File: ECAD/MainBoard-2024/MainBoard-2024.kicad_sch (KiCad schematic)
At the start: 60 parts, among them J1 XT60, J11 Conn_01x03, J12 Conn_01x04, J13 Conn_01x03, J14 Conn_01x03, J16 XT30, J17 XT30, J2 Conn_01x04, J20 BAU, J21 BAU, J22 Conn_01x04, J23 Conn_01x02, J26 BAU, J27 BAU, J28 Conn_01x02, J29 Conn_01x02, J3 ConStep1, J30 Conn_01x03, J5 ConStep1, J6 ConStep1, J7 XT30, J8 Conn_01x02, K2 FINDER-36.11, U1 Teensy3.5_All_Pins, U2 R-78B3.3-2.0, U3 R-78B12-2.0, U4 R-78B5.0-2.0

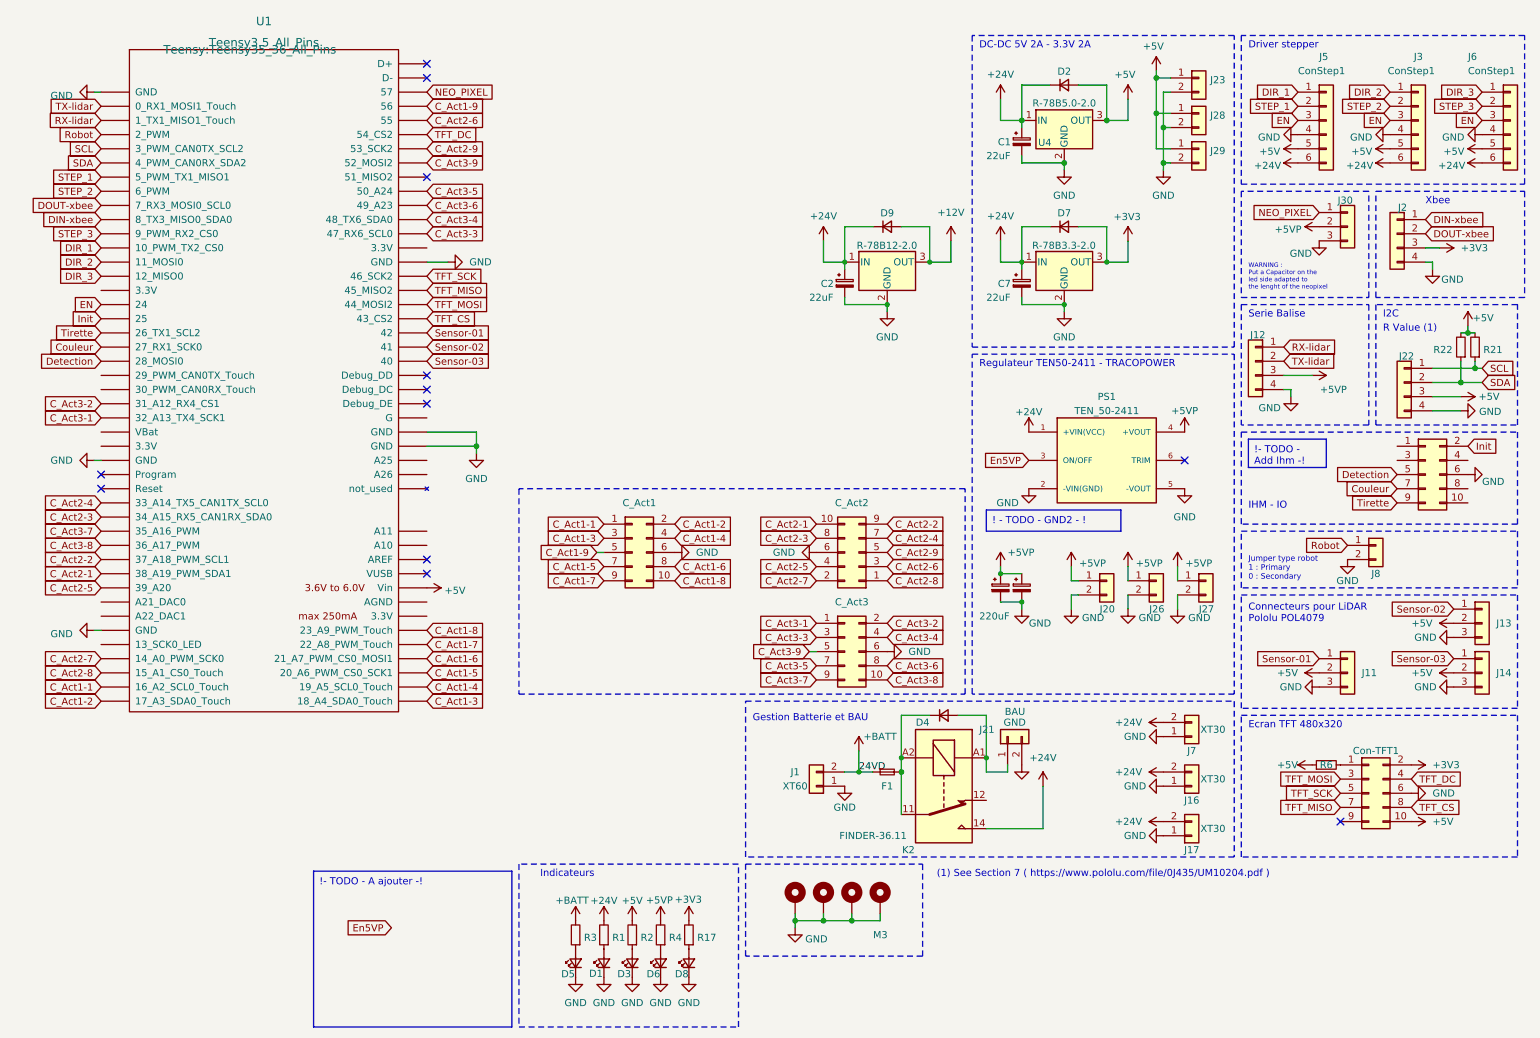
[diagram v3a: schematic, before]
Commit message: add ihm features and 12V connectores
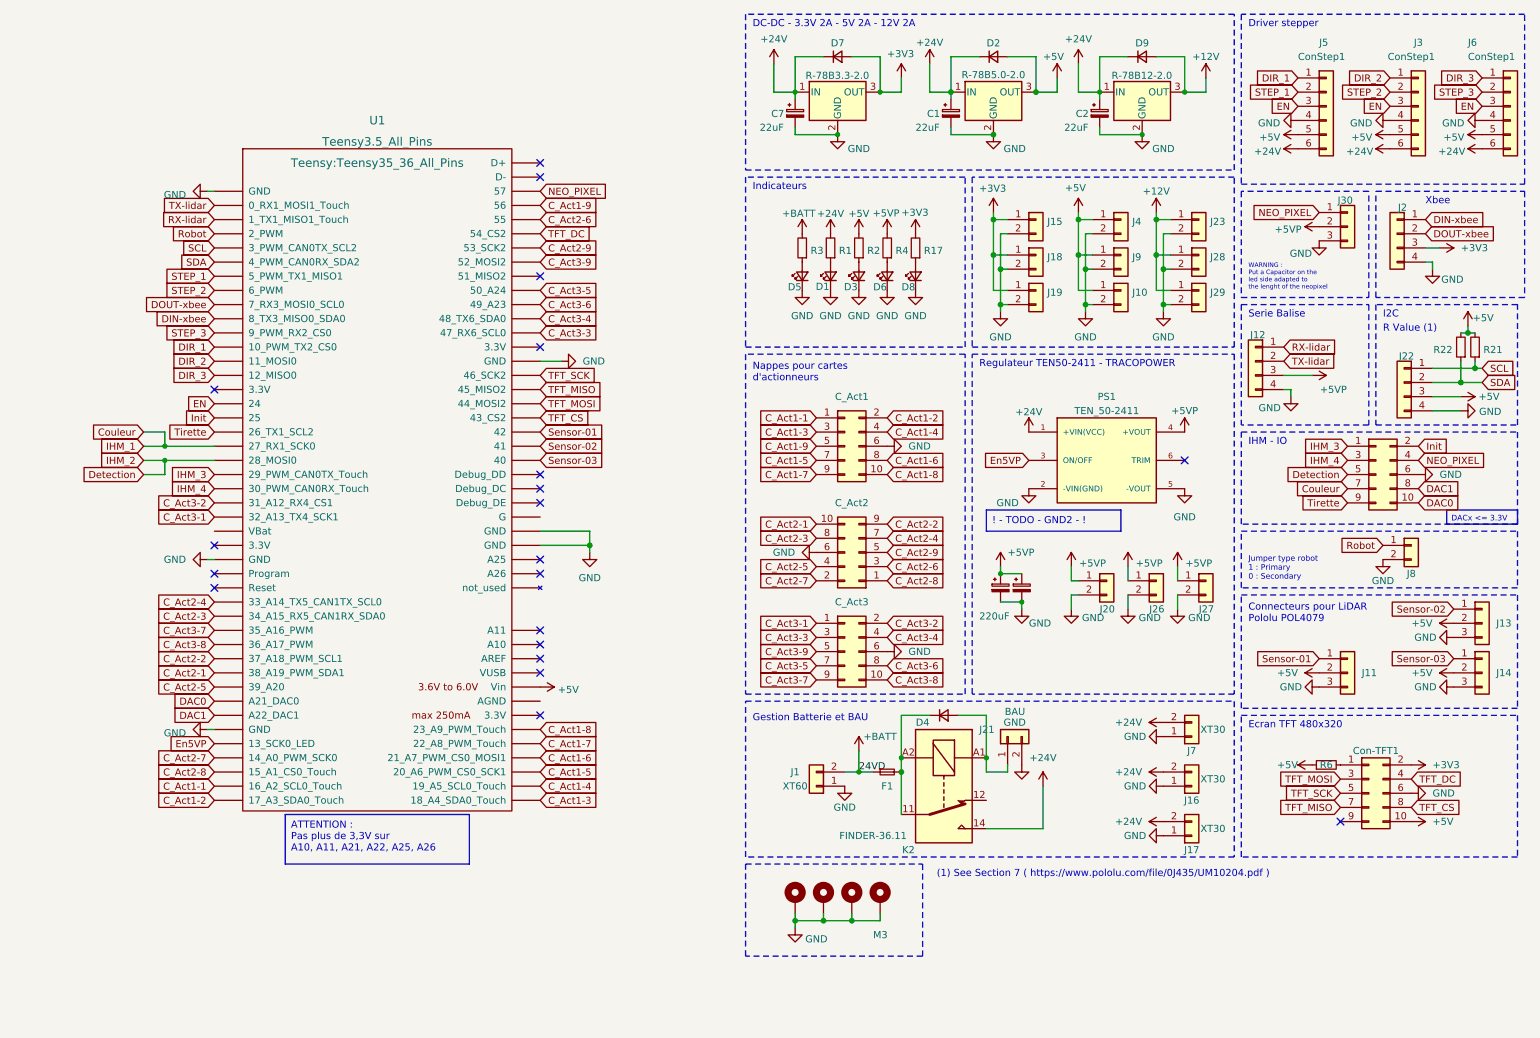
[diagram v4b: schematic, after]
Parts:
- added J10, J15, J18, J19, J4, J9: Conn_01x02, Connector_Molex:Molex_KK-254_AE-6410-02A_1x02_P2.54mm_Vertical, symbol Connector_Generic:Conn_01x02
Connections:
- net +12V: now also J23.1 (Pin_1), J28.1 (Pin_1), J29.1 (Pin_1)
- net +3V3: now also J15.1 (Pin_1), J18.1 (Pin_1), J19.1 (Pin_1)
- net +5V: now also J10.1 (Pin_1), J4.1 (Pin_1), J9.1 (Pin_1); no longer J23.1 (Pin_1), J28.1 (Pin_1), J29.1 (Pin_1)
- net En5VP: now also U1.40 (13_SCK0_LED)
- net GND: now also J10.2 (Pin_2), J15.2 (Pin_2), J18.2 (Pin_2), J19.2 (Pin_2), J4.2 (Pin_2), J9.2 (Pin_2)
- net NEO_PIXEL: now also IHM-IO1.4 (Pin_4)
- net IHM_3: now reaches IHM-IO1.1 (Pin_1)
- net IHM_3: now also U1.21 (29_PWM_CAN0TX_Touch)
- net DAC0: now reaches IHM-IO1.10 (Pin_10)
- net DAC0: now also U1.37 (A21_DAC0)
- net IHM_4: now reaches IHM-IO1.3 (Pin_3)
- net IHM_4: now also U1.22 (30_PWM_CAN0RX_Touch)
- net DAC1: now reaches IHM-IO1.8 (Pin_8)
- net DAC1: now also U1.38 (A22_DAC1)
- no-connect marks 12 -> 20
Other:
- note added: "DC-DC - 3.3V 2A - 5V 2A - 12V 2A"
- note added: "Nappes pour cartes d'actionneurs"
- note removed: "DC-DC 5V 2A - 3.3V 2A"
- moved on the sheet: C1, C2, C7, C_Act1, D1, D2, D3, D5, D6, D7, D8, D9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

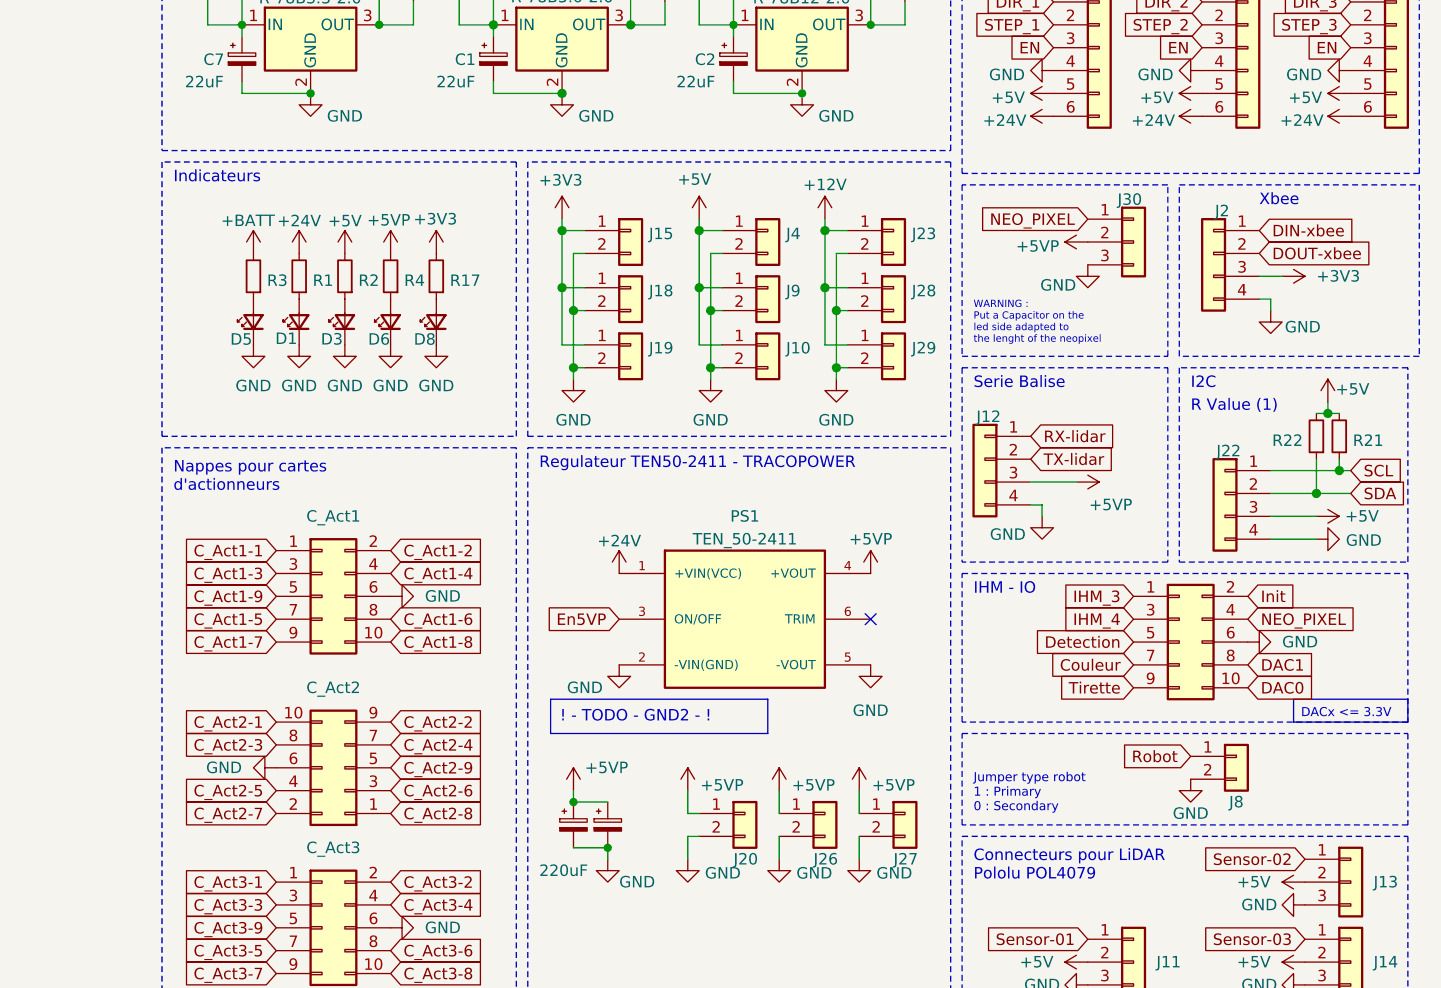
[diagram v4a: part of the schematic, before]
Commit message: Update 3.3V connectors and placements
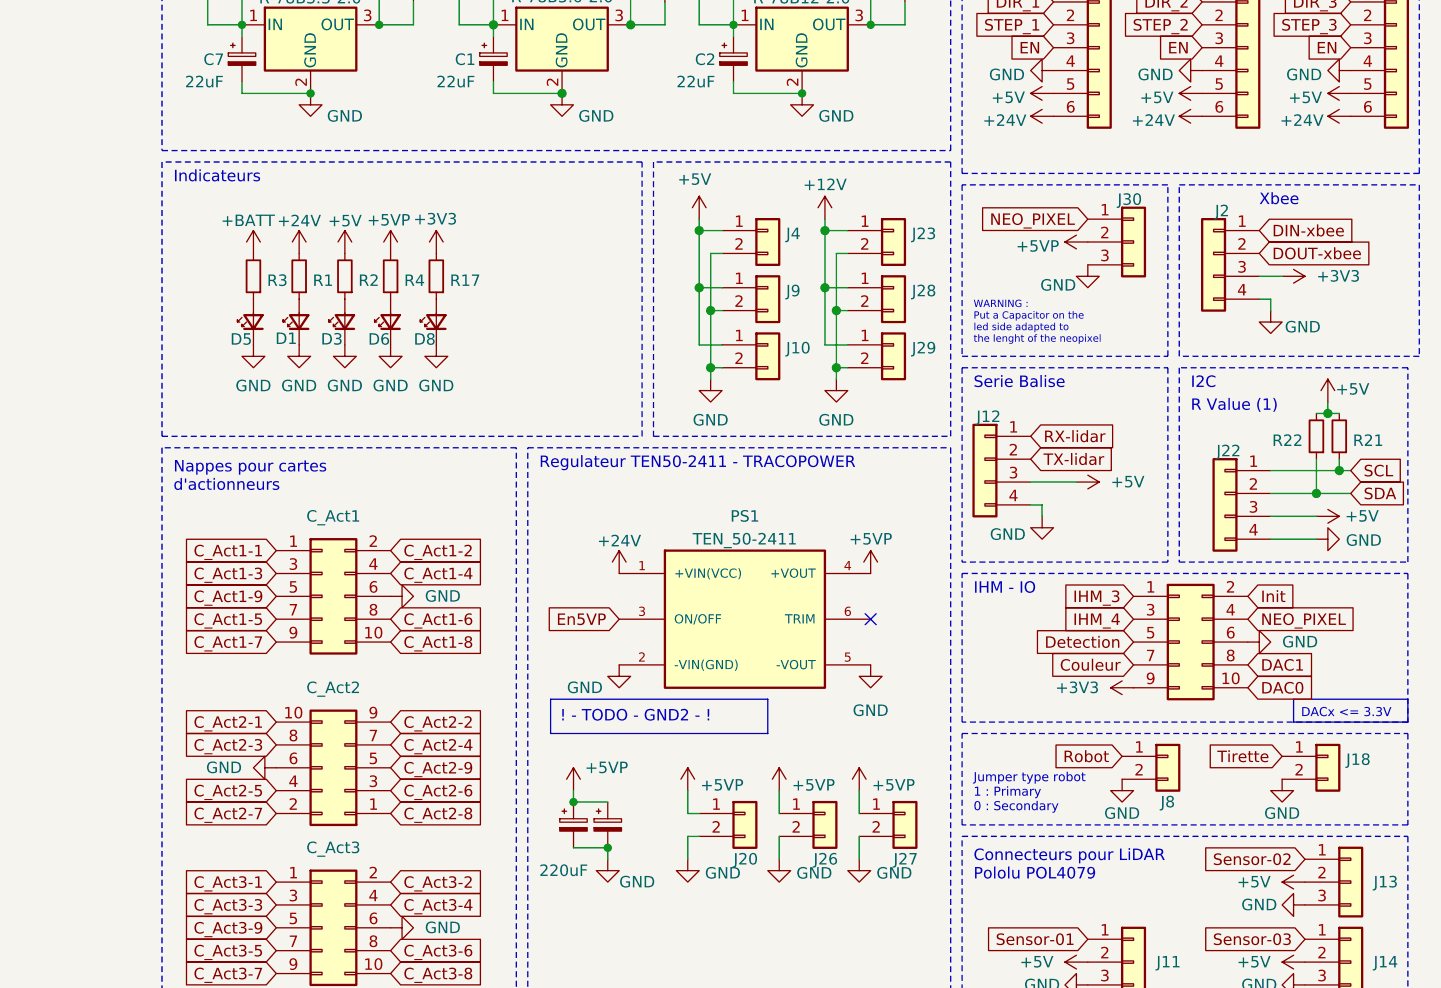
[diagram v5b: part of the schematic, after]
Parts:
- removed J15, J19: Conn_01x02, Connector_Molex:Molex_KK-254_AE-6410-02A_1x02_P2.54mm_Vertical, symbol Connector_Generic:Conn_01x02
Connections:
- net +3V3: now also IHM-IO1.9 (Pin_9); no longer J18.1 (Pin_1)
- net +5V: now also J12.3 (Pin_3)
- net +5VP: no longer J12.3 (Pin_3)
- net Tirette: now also J18.1 (Pin_1); no longer IHM-IO1.9 (Pin_9)
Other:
- moved on the sheet: J8
